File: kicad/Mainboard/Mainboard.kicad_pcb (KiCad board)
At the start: 2 copper layers, 46.9 x 107.1 mm, 255 parts, among them J1 TP1, J10 MIC_EXT, J11 VIB2, J12 SPK_EXT, J13 GPS_CONN, J14 Micro_SD_Card, J15 DBG_CONN, J2 TP2, J3 USB_OTG, J4 SWD, J5 BATT, J6 POT_PWR_SW, J7 Conn_01x10, J8 Antenna, J9 VIB1, Q1 BSS138, Q2 BSS138, Q3 BGA6589, Q4 BSS138, Q5 BSS138, Q6 BSS138, SW1 INT_PTT_SW, T1 AFT05MS004NT1, U1 STM32F777VIT, U10 LM386, U11 LSM9DS1, U12 GD25Q16CSIGTR, U13 LM321, U14 ESP8266EX, U2 USBLC6-2SC6, U3 LD1117S50TR_SOT223, U4 LD1117S33TR_SOT223, U5 ADF7021, U6 HMC546MS8GETR, U7 LM2904A, U8 HEF4066B, U9 OPA340UA, X1 12.288MHz

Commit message: pcb improvement
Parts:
- added AE1: Antenna_Dipole, RF_Antenna:Pulse_W3011, F.Cu at (75.9, 152.5)
- moved R1 94.4 mm to (55.5, 139.4)
- moved C7 6.98 mm to (52.6, 143.4), turned to 90 degrees
- moved J13 5.42 mm to (50.1, 122.4), turned to 0 degrees
- moved U2 5.37 mm to (55.2, 141.9)
- moved D5 5.37 mm to (58.7, 145.8)
- moved J3 5.37 mm to (61.2, 141.5)
- moved L1 5.37 mm to (56.3, 144.9)
- moved J14 5.30 mm to (57.0, 128.8)
- moved C6 5.11 mm to (52.6, 140.4), turned to 270 degrees
- moved C19 5.02 mm to (63.8, 117.3)
- moved C92 5.02 mm to (58.3, 113.0)
- moved R53 5.02 mm to (58.8, 116.8)
- moved R55 5.02 mm to (63.6, 114.6)
- moved R56 5.02 mm to (63.6, 116.8)
- moved U11 5.02 mm to (60.9, 114.0)
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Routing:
- net +3V3: track 262.6 -> 200.6 mm, vias 22 -> 20
- net I2C1_SCL: track 35.7 -> 16.5 mm
- net I2C1_SDA: track 38.0 -> 19.9 mm
- net GPS_EN: track 18.8 -> 3.01 mm
- net UART1_TX: track 17.0 -> 2.92 mm
- net UART1_RX: track 15.5 -> 3.07 mm
- net Net-(C7-Pad2): track 14.8 -> 7.18 mm
- net Net-(C6-Pad2): track 14.4 -> 7.30 mm
- net SWDIO: track 8.20 -> 1.60 mm
- net SD_CMD: track 19.9 -> 13.9 mm
- net SD_D2: track 17.4 -> 11.8 mm
- net SD_D0: track 12.5 -> 17.3 mm
- net SD_CLK: track 15.6 -> 10.9 mm
- net SD_D1: track 11.7 -> 16.3 mm
- net SD_D3: track 16.9 -> 12.4 mm
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
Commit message: more pcb improvements
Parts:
- moved AE1 9.28 mm to (67.0, 155.1)
- moved C103 7.26 mm to (53.9, 163.8)
- moved C102 2.96 mm to (59.1, 152.7)
- moved C99 2.96 mm to (57.6, 152.7)
- moved R62 2.96 mm to (60.6, 152.7)
- moved U14 2.96 mm to (58.6, 154.5)
- moved C100 2.96 mm to (63.5, 153.3)
- moved C13 2.82 mm to (43.6, 155.9), turned to 180 degrees
- moved U12 1.82 mm to (56.3, 158.2), turned to 180 degrees
- moved J11 0.12 mm to (44.7, 164.9)
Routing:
- net PA_RAMP: track 0.00 -> 76.7 mm, vias 0 -> 6
- net +3V3: track 200.6 -> 260.3 mm, vias 20 -> 21
- net +5V: track 181.4 -> 217.3 mm
- net I2C1_SCL: track 16.5 -> 46.4 mm, vias 3 -> 1
- net I2C1_SDA: track 19.9 -> 49.1 mm, vias 3 -> 1
- net UART1_TX: track 2.92 -> 20.6 mm, vias 1 -> 2
- net UART1_RX: track 3.07 -> 19.3 mm
- net GPS_EN: track 3.01 -> 17.4 mm, vias 1 -> 2
- net UART2_RX: track 15.1 -> 2.54 mm
- net SD_CMD: track 13.9 -> 24.7 mm
- net SD_D2: track 11.8 -> 22.5 mm
- net UART2_TX: track 14.8 -> 4.33 mm, vias 2 -> 0
- net WIFI_RST: track 14.9 -> 4.60 mm, vias 2 -> 0
- net SD_CLK: track 10.9 -> 20.5 mm
- net SD_D3: track 12.4 -> 21.9 mm
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
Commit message: Added 2,4GHz antenna; added RF matching Pi circuit; plotted new PDF
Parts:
- removed the C14 at (141.2, 163.2)
- removed the C14 at (67.4, 183.7)
- removed the C16 at (134.1, 190.3)
- removed the C16 at (171.2, 96.6)
- removed the C18 at (142.0, 154.7)
- removed the C18 at (102.6, 170.3)
- removed the C20 at (74.8, 158.7)
- added C104: DNP, Inductor_SMD:L_0402_1005Metric, B.Cu at (63.1, 150.4)
- added C105: DNP, Inductor_SMD:L_0402_1005Metric, B.Cu at (60.3, 150.4)
- added C14: 100n, Capacitor_SMD:C_0603_1608Metric, F.Cu at (76.6, 93.2)
- added C16: 10u/TA, Capacitor_Tantalum_SMD:CP_EIA-3216-18_Kemet-A, F.Cu at (77.5, 103.7)
- added C18: 22u/TA, Capacitor_Tantalum_SMD:CP_EIA-3216-18_Kemet-A, F.Cu at (77.5, 106.8)
- added L15: L, Inductor_SMD:L_0402_1005Metric, B.Cu at (61.7, 150.9)
- added Y1: 24MHz, Crystal:Crystal_SMD_Abracon_ABM10-4Pin_2.5x2.0mm, B.Cu at (56.1, 150.3)
- AE1: value Antenna_Dipole -> Antenna_Chip; footprint RF_Antenna:Pulse_W3011 -> TR-9:RFECA3216060A1T_shifted; moved to B.Cu
- C100: footprint Capacitor_SMD:C_0603_1608Metric -> Inductor_SMD:L_0402_1005Metric; moved to B.Cu
- moved C94 232.6 mm to (60.5, 155.3), turned to 270 degrees
- moved C62 157.1 mm to (96.2, 96.4)
- moved C21 117.7 mm to (92.2, 96.4)
- moved C12 112.5 mm to (93.0, 93.6)
- moved C26 111.3 mm to (97.9, 93.2)
- moved C11 101.0 mm to (106.2, 93.6), turned to 0 degrees
- moved R65 92.5 mm to (80.6, 95.7)
- moved R66 92.5 mm to (84.6, 93.2)
- moved C5 51.5 mm to (91.3, 105.8)
- moved C101 50.8 mm to (58.4, 150.7), turned to 90 degrees
- moved R2 34.9 mm to (95.3, 103.3)
- moved C3 27.7 mm to (91.3, 103.3)
- moved R43 24.3 mm to (80.6, 93.2)
- moved R42 23.8 mm to (76.6, 95.7)
- moved C102 3.36 mm to (56.8, 150.2), turned to 90 degrees
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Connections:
- AE1 pad 2: Net-(AE1-Pad2) -> GND
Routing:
- net +3V3: track 260.3 -> 315.0 mm, vias 21 -> 26
- net PTT: track 36.9 -> 88.5 mm, vias 5 -> 7
- net UART2_RX: track 2.54 -> 12.0 mm, vias 0 -> 2
- net UART2_TX: track 4.33 -> 11.7 mm, vias 0 -> 2
- net Net-(C90-Pad2): track 0.07 -> 6.64 mm
- net WIFI_EN: track 9.81 -> 15.1 mm, vias 1 -> 2
- net Net-(AE1-Pad1): track 0.00 -> 4.34 mm
- net Net-(C99-Pad1): track 1.64 -> 5.66 mm
- net Net-(C100-Pad2): track 0.00 -> 3.15 mm
- net WIFI_RST: track 4.60 -> 2.02 mm
- net GND: track 75.4 -> 72.8 mm, vias 52 -> 51
- net Net-(C102-Pad1): track 1.91 -> 4.03 mm
- net Net-(C100-Pad1): track 0.00 -> 1.45 mm
- net Net-(C96-Pad2): track 4.23 -> 3.41 mm
- net +5V: track 217.3 -> 218.1 mm
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
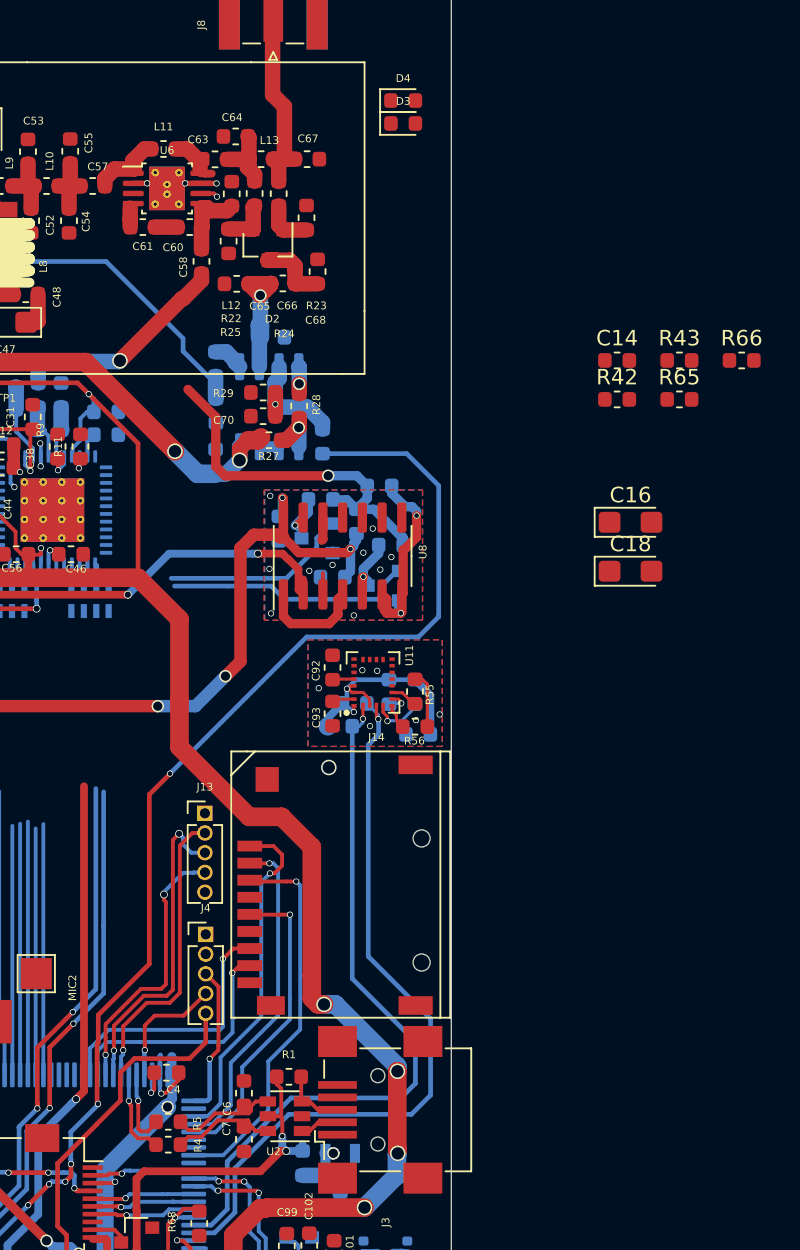
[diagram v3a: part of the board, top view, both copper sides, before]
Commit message: led-s connected
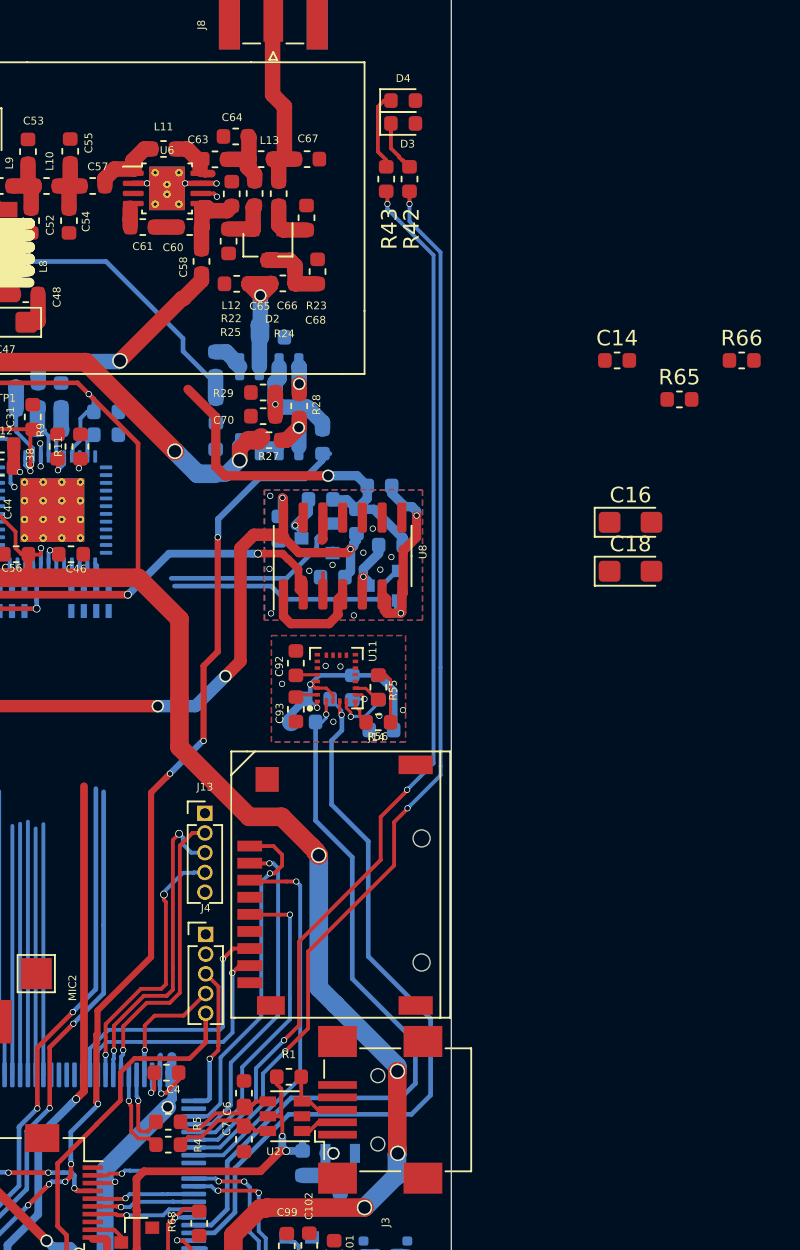
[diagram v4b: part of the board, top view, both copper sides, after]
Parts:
- moved R43 22.2 mm to (61.7, 81.6), turned to 270 degrees
- moved R42 19.5 mm to (63.2, 81.6), turned to 270 degrees
- moved R51 2.38 mm to (61.2, 114.3)
- moved R52 2.38 mm to (59.5, 114.3)
- moved C19 2.38 mm to (61.4, 117.0)
- moved C92 2.38 mm to (55.9, 112.7)
- moved C93 2.38 mm to (55.9, 115.7)
- moved R53 2.38 mm to (56.4, 116.5)
- moved R54 2.38 mm to (57.3, 115.0)
- moved R55 2.38 mm to (61.2, 114.3)
- moved R56 2.38 mm to (61.2, 116.5)
- moved U11 2.38 mm to (58.5, 113.7)
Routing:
- net LED_RED: track 0.00 -> 70.4 mm, vias 0 -> 3
- net LED_GRN: track 0.00 -> 69.6 mm, vias 0 -> 3
- net PA_RAMP: track 76.7 -> 65.6 mm, vias 6 -> 8
- net Net-(D4-Pad1): track 0.00 -> 5.09 mm
- net Net-(D3-Pad1): track 0.00 -> 3.32 mm
- net I2C1_SDA: track 49.1 -> 50.3 mm
- net I2C1_SCL: track 46.4 -> 47.7 mm
- net +3V3: track 315.0 -> 314.7 mm, vias 26 -> 25

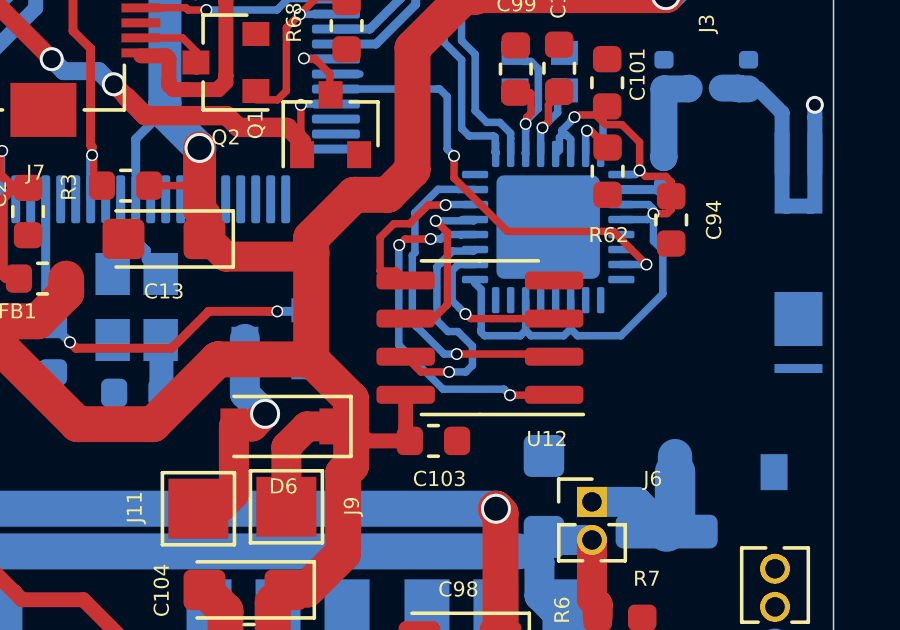
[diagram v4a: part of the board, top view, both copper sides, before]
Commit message: Drawn meanders for flash memory of ESP32 chip. trace difference max +- 0,2mm Added status diodes
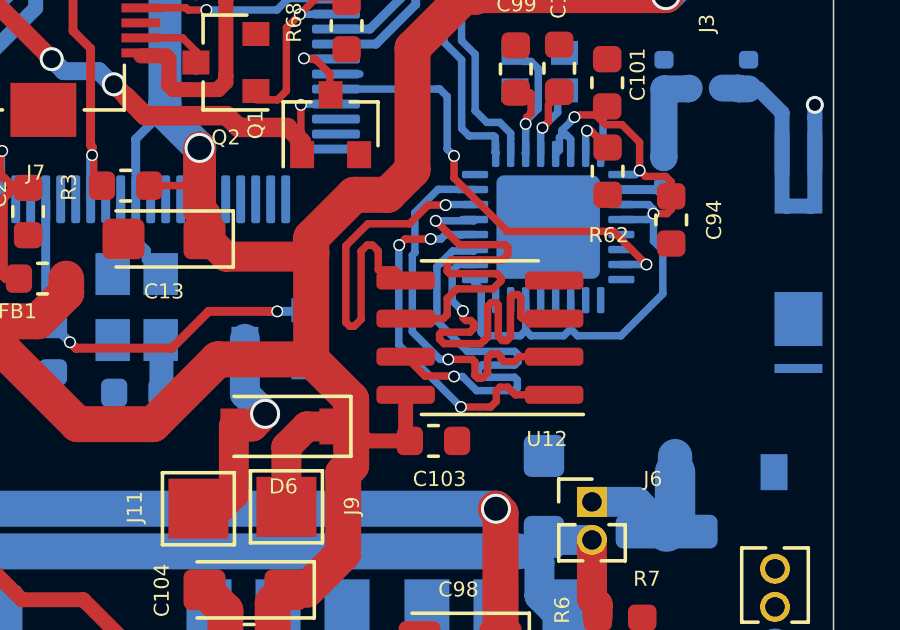
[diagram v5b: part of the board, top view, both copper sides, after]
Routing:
- net MEM_D2: track 5.50 -> 13.4 mm
- net MEM_D0: track 6.52 -> 13.8 mm
- net MEM_CLK: track 6.31 -> 13.2 mm
- net MEM_D3: track 8.05 -> 14.2 mm
- net MEM_D1: track 11.2 -> 13.8 mm
- net MEM_CS: track 11.9 -> 13.3 mm

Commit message: improvement
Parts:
- moved Q1 0.56 mm to (49.7, 151.9)
- moved Q2 0.54 mm to (46.2, 150.1)
- moved R68 0.15 mm to (49.7, 148.6)
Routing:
- net TRX_SW: track 0.00 -> 78.7 mm, vias 0 -> 5
- net +5V: track 218.1 -> 215.1 mm
- net FM_MOD: track 45.7 -> 47.8 mm
- net BLIGHT_CTRL: track 6.86 -> 6.20 mm
- net PTT: track 88.5 -> 88.0 mm

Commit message: a small changes
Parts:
- moved RN1 13.8 mm to (40.3, 122.1)
- moved RN2 13.6 mm to (36.5, 122.1)
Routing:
- net AUDIO_DAC: track 43.4 -> 48.7 mm
- net ADF_SLE: track 16.2 -> 19.2 mm, vias 0 -> 2
- net Net-(RN2-Pad1): track 2.65 -> 0.49 mm
- net ADF_SCLK: track 16.1 -> 17.9 mm, vias 0 -> 2
- net Net-(RN2-Pad3): track 1.50 -> 0.00 mm
- net Net-(RN1-Pad2): track 1.46 -> 0.00 mm
- net Net-(RN2-Pad2): track 1.86 -> 0.43 mm
- net Net-(RN2-Pad4): track 1.37 -> 0.00 mm
- net Net-(RN1-Pad1): track 1.36 -> 0.00 mm
- net ADF_SREAD: track 15.9 -> 17.1 mm, vias 0 -> 2
- net Net-(RN1-Pad4): track 1.96 -> 0.74 mm
- net Net-(RN1-Pad3): track 1.59 -> 0.45 mm
- net ADF_SDATA: track 16.3 -> 17.1 mm, vias 0 -> 1

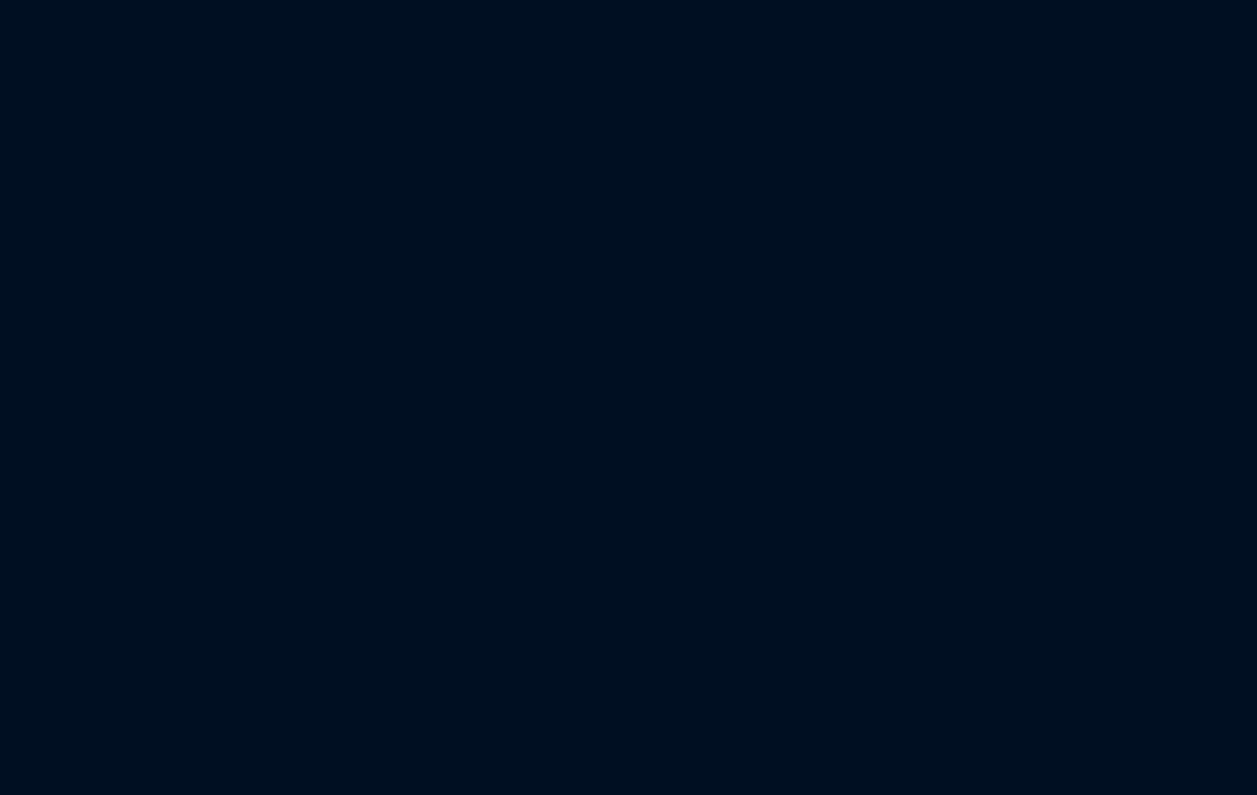
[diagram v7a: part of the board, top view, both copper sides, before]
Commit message: added 6 testpoints
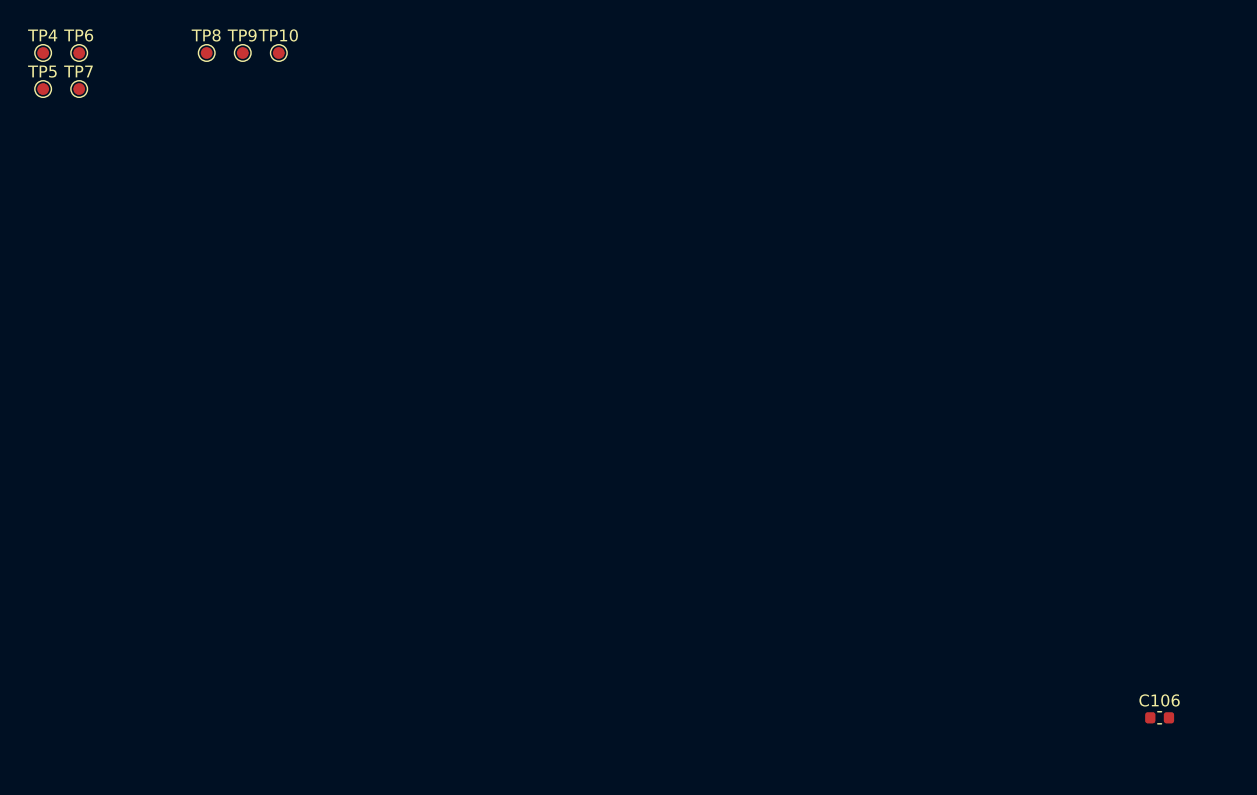
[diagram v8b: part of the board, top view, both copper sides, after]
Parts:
- added C106: 10p, Capacitor_SMD:C_0603_1608Metric, F.Cu at (-82.3, 20.4)
- added TP10: TestPoint_Probe, TestPoint:TestPoint_Pad_D1.0mm, F.Cu at (-156.8, -35.8)
- added TP4: TestPoint_Probe, TestPoint:TestPoint_Pad_D1.0mm, F.Cu at (-176.8, -35.8)
- added TP5: TestPoint_Probe, TestPoint:TestPoint_Pad_D1.0mm, F.Cu at (-176.8, -32.8)
- added TP6: TestPoint_Probe, TestPoint:TestPoint_Pad_D1.0mm, F.Cu at (-173.7, -35.8)
- added TP7: TestPoint_Probe, TestPoint:TestPoint_Pad_D1.0mm, F.Cu at (-173.7, -32.8)
- added TP8: TestPoint_Probe, TestPoint:TestPoint_Pad_D1.0mm, F.Cu at (-162.9, -35.8)
- added TP9: TestPoint_Probe, TestPoint:TestPoint_Pad_D1.0mm, F.Cu at (-159.9, -35.8)
- R26: value 1k -> 10k
